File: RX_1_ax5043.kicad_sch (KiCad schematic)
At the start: 19 parts, among them P5 CONUFL001-SMD-T, Q3 DMP2160UWQ-7, U21 AX5043

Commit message: Add licensing
Use CERN-OHL-W version 2

Signed-off-by: Corey Minyard <corey@minyard.net>
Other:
- note removed: "RECEIVER 1"
- title: Radiation Tolerant PacSat Communication -> AX5043 Receiver 1
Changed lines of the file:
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@@
 	(paper "USLedger")
 	(title_block
-		(title "Radiation Tolerant PacSat Communication")
-		(date "2023-06-17")
-		(rev "A")
+		(title "AX5043 Receiver 1")
+		(date "2026-08-20")
+		(rev "4.0")
 		(company "AMSAT-NA")
-		(comment 1 "N5BRG")
-	)
-	(text "RECEIVER 1"
-		(exclude_from_sim no)
-		(at 336.55 247.65 0)
-		(effects
-			(font
-				(size 6.096 6.096)
-			)
-			(justify left bottom)
-		)
+		(comment 1 "AE5KM")
+		(comment 2 "Copyright Corey Minyard, 2026")
+		(comment 3 "Licensed under CERN-OHL-W version 2")
 	)
 	(text "The cover for this frame is 2118713-4\nand also needs to be ordered.  When access\nto the parts is no longer needed (or shake\nresistance is required) the 2118706-4 has\nthe same layout as a single unit.\n\nThis is the same for all shields on the\nAX5043 parts."

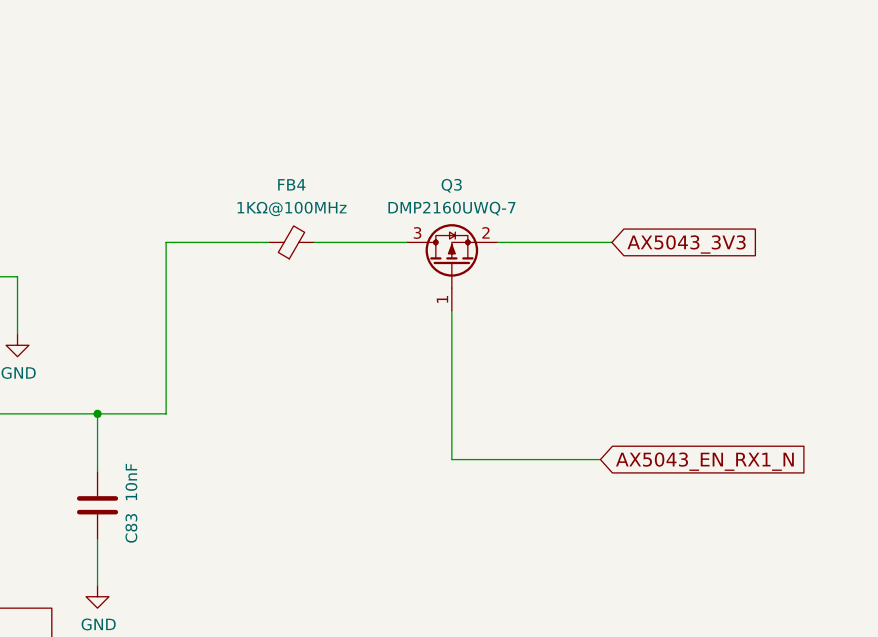
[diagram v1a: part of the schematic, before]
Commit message: Cost reduce the AX5043 power control
Change the MOSFET + ferrite bead combo on all the AX5043 power inputs
to a inrush-controlled power controller.  The space-rated ferrites are
just too expensive.

Signed-off-by: Corey Minyard <corey@minyard.net>
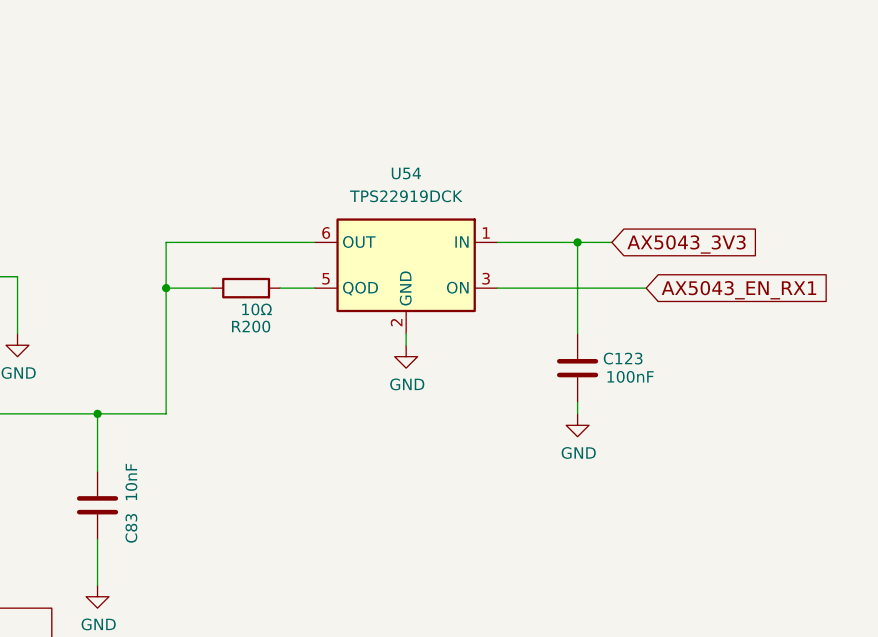
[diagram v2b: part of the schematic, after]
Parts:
- removed FB4: 1KΩ@100MHz, Inductor_SMD:L_0603_1608Metric_Pad1.05x0.95mm_HandSolder, symbol Device:FerriteBead_Small
- removed Q3: DMP2160UWQ-7, Package_TO_SOT_SMD:SOT-323_SC-70, symbol Transistor_FET:Q_PMOS_GSD
- added C123: 100nF, Capacitor_SMD:C_0402_1005Metric_Pad0.74x0.62mm_HandSolder, symbol Device:C
- added R200: 10Ω, Resistor_SMD:R_0402_1005Metric_Pad0.72x0.64mm_HandSolder, symbol Device:R
- added U54: TPS22919DCK, Package_TO_SOT_SMD:SOT-363_SC-70-6, symbol Power_Management:TPS22919DCK
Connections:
- net AX5043_3V3: now also C123.1, U54.1 (IN)
- net GND: now also C123.2, U54.2 (GND)
- net at C83.1, U21.23 (VDD_IO): now also R200.1, U54.6 (OUT)
- new net: R200.2, U54.5 (QOD)
- new net AX5043_EN_RX1: U54.3 (ON)

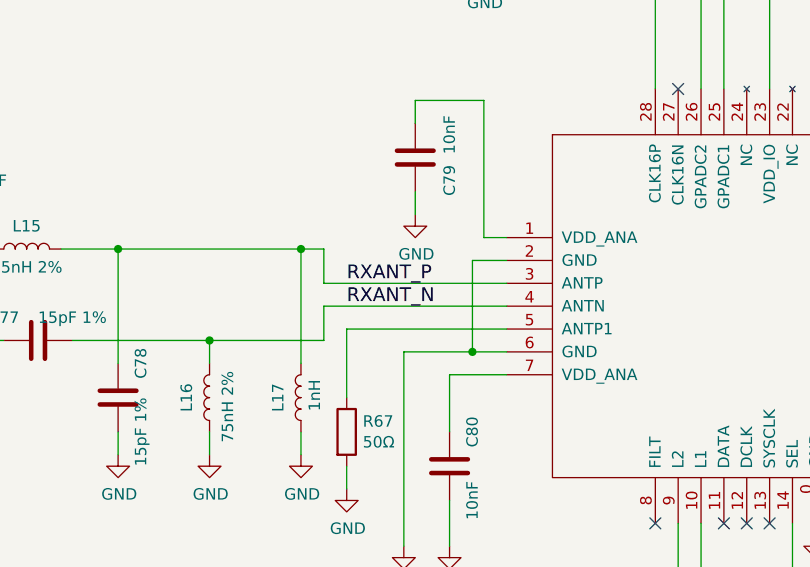
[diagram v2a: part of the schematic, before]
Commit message: Fix clearance around differential pairs
Meet the 5X requirement for trace width vs clearance.

Signed-off-by: Corey Minyard <corey@minyard.net>
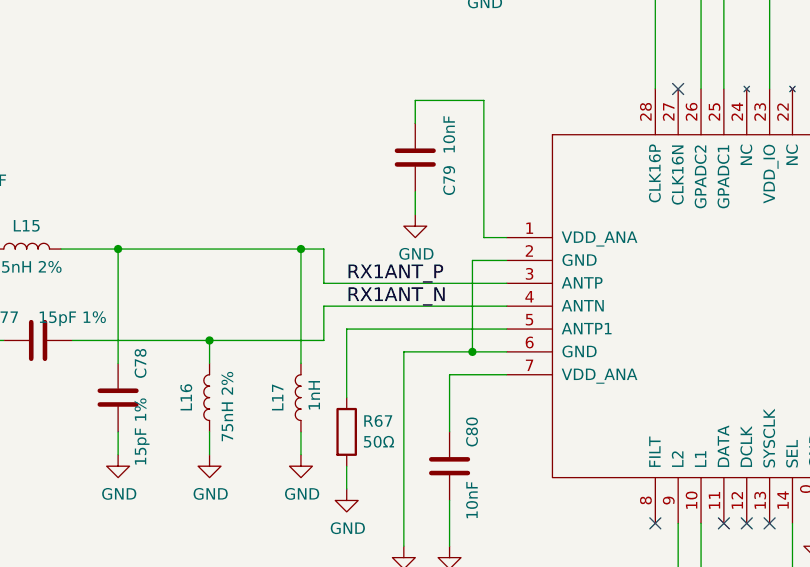
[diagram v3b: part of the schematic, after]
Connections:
- net RXANT_N renamed RX1ANT_N
- net RXANT_P renamed RX1ANT_P
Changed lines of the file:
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@@
 		)
 	)
-	(label "RXANT_N"
+	(label "RX1ANT_N"
 		(at 179.07 135.89 0)
 		(effects
@@
 		)
 	)
-	(label "RXANT_P"
+	(label "RX1ANT_P"
 		(at 179.07 133.35 0)
 		(effects

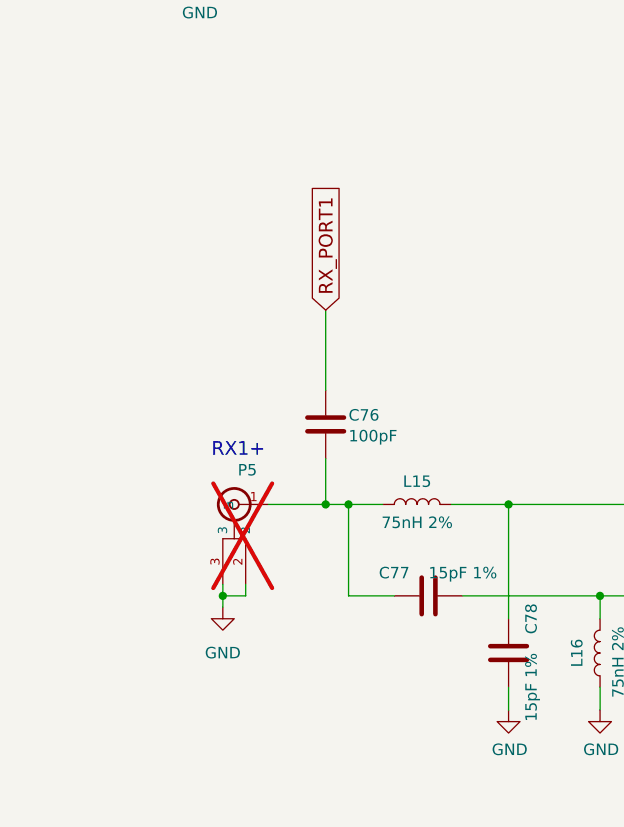
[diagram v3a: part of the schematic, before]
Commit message: Remove U.FL connectors from all AX5043 RX connections except AX5043 4
They aren't necessary.  If you need to pull off an RX line for another
board, you can use 4, and you can use 4 for testing.

Signed-off-by: Corey Minyard <corey@minyard.net>
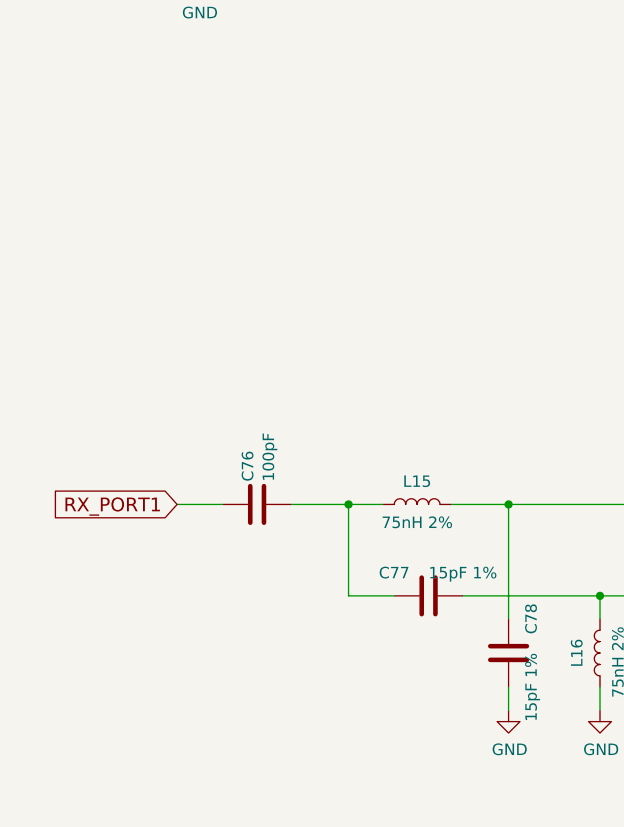
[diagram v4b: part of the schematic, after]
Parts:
- removed P5: CONUFL001-SMD-T, PacSatDev_misc:CONN1_CONUFL_TEC, symbol PACSAT_DEV_misc:U_FL
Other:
- note removed: "RX1+"
- moved on the sheet: C76
